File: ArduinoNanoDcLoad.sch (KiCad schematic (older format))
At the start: 30 parts, among them P1 CONN_01X15, P2 CONN_01X15, Q1 IRFP250N, U1 LMC6484

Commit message: * updated schematic
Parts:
- added C4: 10µ, Capacitors_ThroughHole:C_Radial_D10_L20_P5, symbol CP
- added C5, C7: 100n, Capacitors_ThroughHole:C_Rect_L4_W2.5_P2.5, symbol C
- added D2: 5,1V, Diodes_ThroughHole:Diode_DO-35_SOD27_Horizontal_RM10, symbol ZENER
- added P1: DCLOAD+, Connect:Banana_Jack_1Pin, symbol CONN_01X01
- added P2: DCLOAD-, Connect:Banana_Jack_1Pin, symbol CONN_01X01
- added R14: 10, Resistors_ThroughHole:Resistor_Horizontal_RM15mm, symbol R
- C1: footprint (none) -> Capacitors_ThroughHole:C_Radial_D10_L20_P5
- C2: value 100µ -> 100n; footprint (none) -> Capacitors_ThroughHole:C_Rect_L4_W2.5_P2.5
- C3: footprint (none) -> Capacitors_ThroughHole:C_Rect_L4_W2.5_P2.5
- C6: renamed from C4; footprint (none) -> Capacitors_ThroughHole:C_Rect_L4_W2.5_P2.5
- D1: footprint (none) -> Diodes_ThroughHole:Diode_DO-35_SOD27_Horizontal_RM10
- P3: renamed from P1; footprint (none) -> Pin_Headers:Pin_Header_Straight_1x15
- P4: renamed from P2; footprint (none) -> Pin_Headers:Pin_Header_Straight_1x15
- Q1: footprint (none) -> TO_SOT_Packages_THT:TO-247_Horizontal_Neutral123_largePads
- R1, R10, R11, R12, R13, R2, R3, R4, R8, R9: footprint (none) -> Resistors_ThroughHole:Resistor_Horizontal_RM15mm
- R15: renamed from R14; footprint (none) -> Resistors_ThroughHole:Resistor_Horizontal_RM15mm
- R16: renamed from R15; footprint (none) -> Resistors_ThroughHole:Resistor_Horizontal_RM15mm
- R17: renamed from R16; footprint (none) -> Resistors_ThroughHole:Resistor_Horizontal_RM15mm
- R18: renamed from R17; footprint (none) -> Resistors_ThroughHole:Resistor_Horizontal_RM15mm
- R19: renamed from R18; footprint (none) -> Resistors_ThroughHole:Resistor_Horizontal_RM15mm
- R20: renamed from R19; footprint (none) -> Resistors_ThroughHole:Resistor_Horizontal_RM15mm
- R21: renamed from R20; footprint (none) -> Resistors_ThroughHole:Resistor_Horizontal_RM15mm
- R22: renamed from R21; footprint (none) -> Resistors_ThroughHole:Resistor_Horizontal_RM15mm
- R5: renamed from R6; footprint (none) -> Resistors_ThroughHole:Resistor_Horizontal_RM15mm
- R6: renamed from R7; footprint (none) -> Resistors_ThroughHole:Resistor_Horizontal_RM15mm
- R7: renamed from R5; footprint (none) -> Resistors_ThroughHole:Resistor_Horizontal_RM15mm
- U1: footprint (none) -> Housings_DIP:DIP-14_W7.62mm_LongPads
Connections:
- net ADC_SPANNUNG is gone; now on net ADC7: C6.1, D1.1 (K), R18.1, R19.2
- net ADC_STROM is gone; now on net ADC6: R22.1
- net PWM_PIN9 is gone; now on net OC1A/PB1: R1.2
- net 3V3: now also P4.14 (P14); no longer P4.2 (P2)
- net 5V: now also P4.4 (P4); no longer P4.12 (P12)
- net ADC0/PC0: now also P4.12 (P12); no longer P4.4 (P4)
- net ADC1/PC1: now also P4.11 (P11); no longer P4.5 (P5)
- net ADC2/PC2: now also P4.10 (P10); no longer P4.6 (P6)
- net ADC3/PC3: now also P4.9 (P9); no longer P4.7 (P7)
- net ADC5/PC5/SCL: now also P4.7 (P7); no longer P4.9 (P9)
- net ADC6: now also P4.6 (P6), R21.1, R22.2, U1.8, C7.1, D2.1 (K); no longer P4.10 (P10)
- net ADC7: now also P4.5 (P5); no longer P4.11 (P11)
- net AREF: now also P4.13 (P13); no longer P4.3 (P3)
- net GND: now also P4.2 (P2), C5.2, C7.2, D2.2 (A), P2.1 (P1), R14.2; no longer P4.14 (P14)
- net RESET/PC6: now also P4.3 (P3); no longer P4.13 (P13)
- net SCK/PB5: now also P4.15 (P15); no longer P4.1 (P1)
- net VIN: now also P4.1 (P1); no longer P4.15 (P15)
- net LOAD_DC+: no longer names the net of Q1.2 (D), R18.2
- net LOAD_DC+: now also C4.1, C5.1, P1.1 (P1)
- new net: C4.2, R14.1
- no-connect marks 28 -> 23
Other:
- moved on the sheet: C6, D1, P3, P4, R18, R19, R22

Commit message: * updated
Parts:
- renumbered R15 to R14, R16 to R15, R17 to R16, R14 to R17
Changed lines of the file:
@@
 $EndComp
 $Comp
-L R R15
+L R R14
 U 1 1 5837BE8D
 P 5150 4250
-F 0 "R15" V 5230 4250 50  0000 C CNN
+F 0 "R14" V 5230 4250 50  0000 C CNN
 F 1 "1" V 5150 4250 50  0000 C CNN
 F 2 "Resistors_ThroughHole:Resistor_Horizontal_RM15mm" V 5080 4250 50  0001 C CNN
@@
 $EndComp
 $Comp
-L R R16
+L R R15
 U 1 1 5837BED2
 P 5300 4250
-F 0 "R16" V 5380 4250 50  0000 C CNN
+F 0 "R15" V 5380 4250 50  0000 C CNN
 F 1 "1" V 5300 4250 50  0000 C CNN
 F 2 "Resistors_ThroughHole:Resistor_Horizontal_RM15mm" V 5230 4250 50  0001 C CNN
@@
 $EndComp
 $Comp
-L R R17
+L R R16
 U 1 1 5837BF94
 P 5450 4250
-F 0 "R17" V 5530 4250 50  0000 C CNN
+F 0 "R16" V 5530 4250 50  0000 C CNN
 F 1 "1" V 5450 4250 50  0000 C CNN
 F 2 "Resistors_ThroughHole:Resistor_Horizontal_RM15mm" V 5380 4250 50  0001 C CNN
@@
 $EndComp
 $Comp
-L R R14
+L R R17
 U 1 1 5838940C
 P 5050 2300
-F 0 "R14" V 5130 2300 50  0000 C CNN
+F 0 "R17" V 5130 2300 50  0000 C CNN
 F 1 "10" V 5050 2300 50  0000 C CNN
 F 2 "Resistors_ThroughHole:Resistor_Horizontal_RM15mm" V 4980 2300 50  0001 C CNN

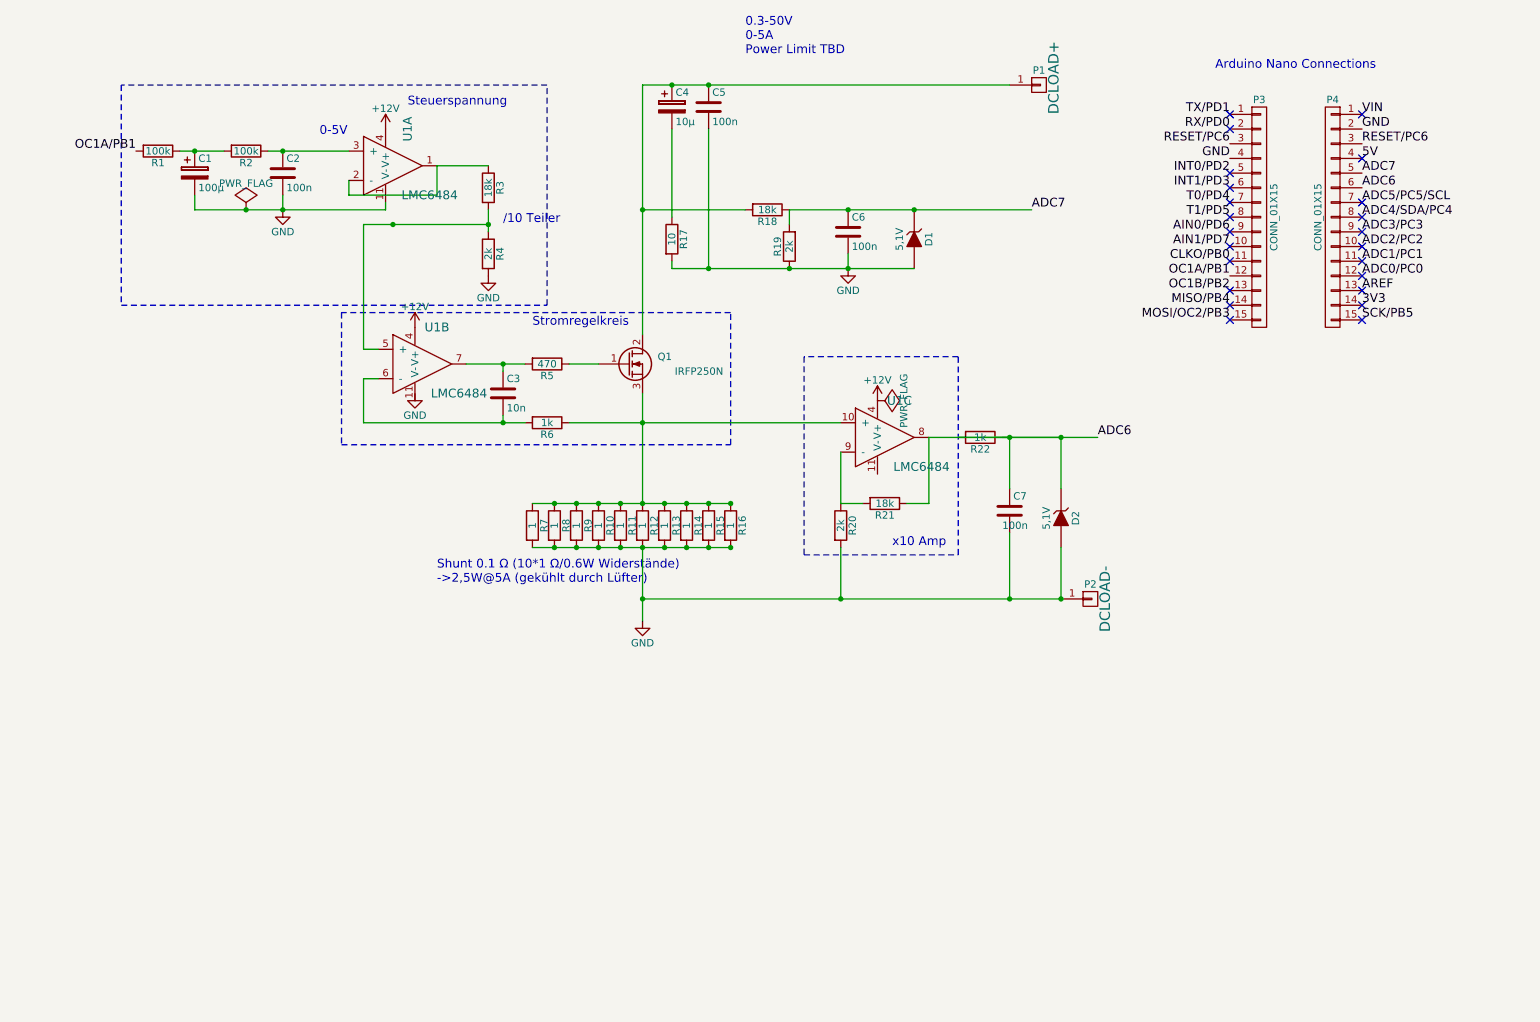
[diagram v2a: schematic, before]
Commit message: * added basic power supply * added LCD
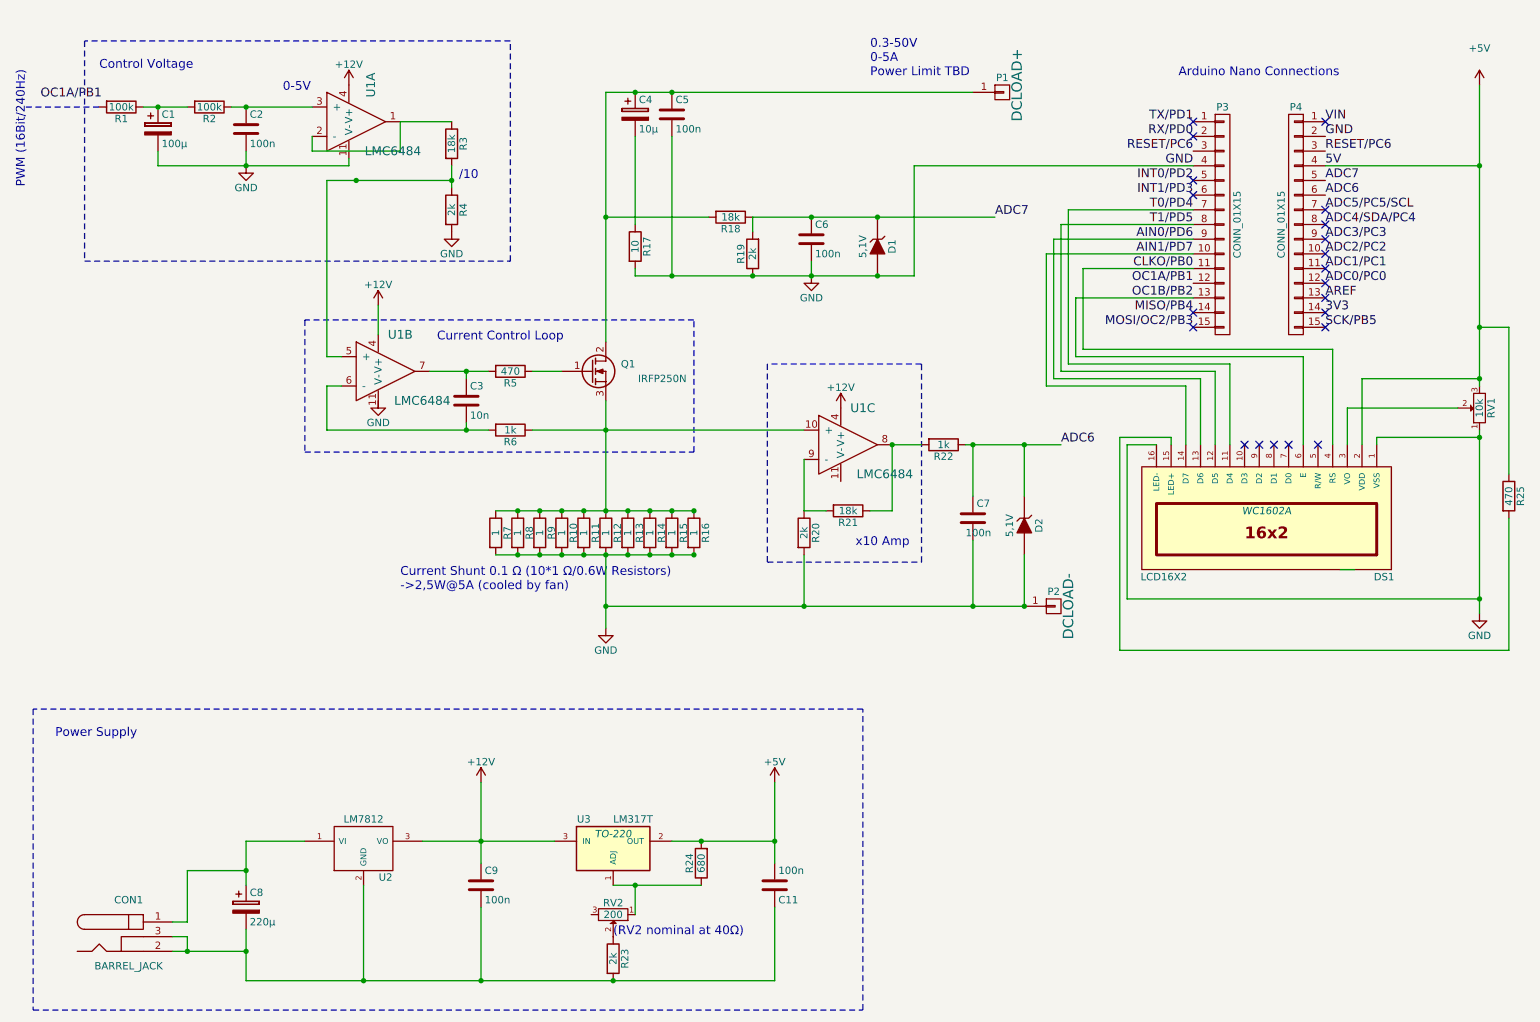
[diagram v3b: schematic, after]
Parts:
- added C11, C9: 100n, symbol C
- added C8: 220µ, symbol CP
- added CON1: BARREL_JACK, symbol BARREL_JACK
- added DS1: LCD16X2, WC1602A, symbol LCD16X2
- added R23: 2k, symbol R
- added R24: 680, symbol R
- added R25: 470, symbol R
- added RV1: 10k, symbol POT
- added RV2: 200, symbol POT
- added U2: LM7812, symbol LM7812
- added U3: LM317T, TO-220, symbol LM317T
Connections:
- net +12V: now also C9.1, U2.3 (VO), U3.3 (IN)
- net ADC6: no longer R21.1, R22.2, U1.8
- net AIN0/PD6: now also DS1.13 (D6)
- net AIN1/PD7: now also DS1.14 (D7)
- net CLKO/PB0: now also DS1.4 (RS)
- net GND: now also DS1.1 (VSS), DS1.16 (LED-), RV1.1
- net OC1A/PB1: no longer R1.2
- net OC1B/PB2: now also DS1.6 (E)
- net T0/PD4: now also DS1.11 (D4)
- net T1/PD5: now also DS1.12 (D5)
- net 5V renamed +5V
- net +5V: now also C11.2, DS1.2 (VDD), R24.2, R25.1, RV1.3, U3.2 (OUT)
- new net: R21.1, R22.2, U1.8
- new net: DS1.15 (LED+), R25.2
- new net: DS1.3 (VO), RV1.2
- new net: C8.1, CON1.1, U2.1 (VI)
- new net: C11.1, C8.2, C9.2, CON1.2, CON1.3, R23.2, U2.2 (GND)
- new net: R24.1, RV2.1, U3.1 (ADJ)
- new net: R23.1, RV2.2
- no-connect marks 23 -> 21
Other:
- note added: "(RV2 nominal at 40Ω)"
- note added: "/10"
- note added: "Control Voltage"
- note added: "Current Control Loop"
- note added: "Current Shunt 0.1 Ω (10*1 Ω/0.6W Resistors)\n->2,5W@5A (cooled by fan)\n"
- note added: "PWM (16Bit/240Hz)"
- note added: "Power Supply"
- note removed: "/10 Teiler"
- note removed: "Shunt 0.1 Ω (10*1 Ω/0.6W Widerstände)\n->2,5W@5A (gekühlt durch Lüfter)\n"
- note removed: "Steuerspannung"
- note removed: "Stromregelkreis"
- moved on the sheet: C1, C2, C3, C4, C5, C6, C7, D1, D2, P1, P2, P3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

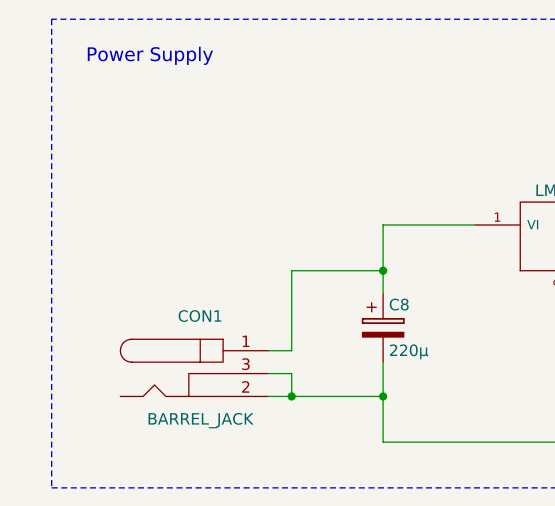
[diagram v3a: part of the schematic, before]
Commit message: added comment to schematic
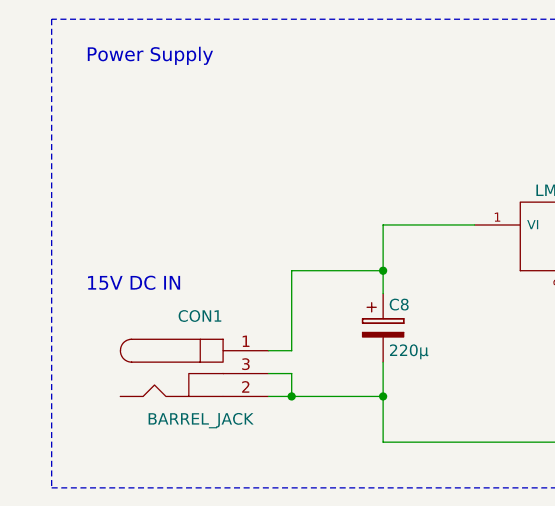
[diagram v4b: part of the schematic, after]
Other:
- note added: "15V DC IN"
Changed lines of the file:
@@
 	1750 6600 2150 6600
 Connection ~ 2150 6600
+Text Notes 850  6700 0    60   ~ 0
+15V DC IN
 $EndSCHEMATC

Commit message: * updated pcb layout
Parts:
- C11, C9: footprint (none) -> Capacitors_ThroughHole:C_Rect_L4_W2.5_P2.5
- C8: footprint (none) -> Capacitors_ThroughHole:C_Radial_D10_L20_P5
- CON1: footprint (none) -> Connect:JACK_ALIM
- DS1: footprint WC1602A -> Display:WC1602A
- R23, R24, R25: footprint (none) -> Resistors_ThroughHole:Resistor_Horizontal_RM15mm
- RV1, RV2: footprint (none) -> Potentiometers:Potentiometer_Trimmer-Piher-PT15-h5_vertical
- U2: footprint (none) -> TO_SOT_Packages_THT:TO-220_Neutral123_Vertical
- U3: footprint TO-220 -> TO_SOT_Packages_THT:TO-220_Neutral123_Vertical
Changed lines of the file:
@@
 	3550 1800 3550 1950
 $Comp
-L GND #PWR5
+L GND #PWR01
 U 1 1 5837A18E
 P 3550 2250
-F 0 "#PWR5" H 3550 2000 50  0001 C CNN
+F 0 "#PWR01" H 3550 2000 50  0001 C CNN
 F 1 "GND" H 3550 2100 50  0000 C CNN
 F 2 "" H 3550 2250 50  0000 C CNN
@@
 Connection ~ 3550 1900
 $Comp
-L GND #PWR9
+L GND #PWR02
 U 1 1 5837A566
 P 6000 2550
-F 0 "#PWR9" H 6000 2300 50  0001 C CNN
+F 0 "#PWR02" H 6000 2300 50  0001 C CNN
 F 1 "GND" H 6000 2400 50  0000 C CNN
 F 2 "" H 6000 2550 50  0000 C CNN
@@
 	4600 4450 4600 4950
 $Comp
-L GND #PWR7
+L GND #PWR03
 U 1 1 5837E175
 P 4600 4950
-F 0 "#PWR7" H 4600 4700 50  0001 C CNN
+F 0 "#PWR03" H 4600 4700 50  0001 C CNN
 F 1 "GND" H 4600 4800 50  0000 C CNN
 F 2 "" H 4600 4950 50  0000 C CNN
@@
 	3200 1700 3200 1500
 $Comp
-L GND #PWR1
+L GND #PWR04
 U 1 1 5838A7B7
 P 2150 1800
-F 0 "#PWR1" H 2150 1550 50  0001 C CNN
+F 0 "#PWR04" H 2150 1550 50  0001 C CNN
 F 1 "GND" H 2150 1650 50  0000 C CNN
 F 2 "" H 2150 1800 50  0000 C CNN
@@
 $EndComp
 $Comp
-L +12V #PWR2
+L +12V #PWR05
 U 1 1 5838A825
 P 2850 1250
-F 0 "#PWR2" H 2850 1100 50  0001 C CNN
+F 0 "#PWR05" H 2850 1100 50  0001 C CNN
 F 1 "+12V" H 2850 1390 50  0000 C CNN
 F 2 "" H 2850 1250 50  0000 C CNN
@@
 $EndComp
 $Comp
-L +12V #PWR10
+L +12V #PWR06
 U 1 1 5838A875
 P 6200 3450
-F 0 "#PWR10" H 6200 3300 50  0001 C CNN
+F 0 "#PWR06" H 6200 3300 50  0001 C CNN
 F 1 "+12V" H 6200 3590 50  0000 C CNN
 F 2 "" H 6200 3450 50  0000 C CNN
@@
 $EndComp
 $Comp
-L GND #PWR4
+L GND #PWR07
 U 1 1 5838AB96
 P 3050 3400
-F 0 "#PWR4" H 3050 3150 50  0001 C CNN
+F 0 "#PWR07" H 3050 3150 50  0001 C CNN
 F 1 "GND" H 3050 3250 50  0000 C CNN
 F 2 "" H 3050 3400 50  0000 C CNN
@@
 $EndComp
 $Comp
-L +12V #PWR3
+L +12V #PWR08
 U 1 1 5838AC69
 P 3050 2750
-F 0 "#PWR3" H 3050 2600 50  0001 C CNN
+F 0 "#PWR08" H 3050 2600 50  0001 C CNN
 F 1 "+12V" H 3050 2890 50  0000 C CNN
 F 2 "" H 3050 2750 50  0000 C CNN
@@
 F 0 "DS1" H 8300 4600 50  0000 C CNN
 F 1 "LCD16X2" H 9800 4600 50  0000 C CNN
-F 2 "WC1602A" H 9100 4150 50  0000 C CIN
+F 2 "Display:WC1602A" H 9100 4150 50  0000 C CIN
 F 3 "" H 9100 4200 50  0000 C CNN
 	1    9100 4200
@@
 $EndComp
 $Comp
-L +5V #PWR11
+L +5V #PWR09
 U 1 1 583D9119
 P 10550 1250
-F 0 "#PWR11" H 10550 1100 50  0001 C CNN
+F 0 "#PWR09" H 10550 1100 50  0001 C CNN
 F 1 "+5V" H 10550 1500 50  0000 C CNN
 F 2 "" H 10550 1250 50  0000 C CNN
@@
 F 0 "RV1" H 10550 3370 50  0000 C CNN
 F 1 "10k" H 10550 3450 50  0000 C CNN
-F 2 "" H 10550 3450 50  0000 C CNN
+F 2 "Potentiometers:Potentiometer_Trimmer-Piher-PT15-h5_vertical" H 10550 3450 50  0001 C CNN
 F 3 "" H 10550 3450 50  0000 C CNN
 	1    10550 3450
@@
 	9600 4550 9700 4550
 $Comp
-L GND #PWR12
+L GND #PWR010
 U 1 1 583DB5FD
 P 10550 4850
-F 0 "#PWR12" H 10550 4600 50  0001 C CNN
+F 0 "#PWR010" H 10550 4600 50  0001 C CNN
 F 1 "GND" H 10550 4700 50  0000 C CNN
 F 2 "" H 10550 4850 50  0000 C CNN
@@
 F 0 "CON1" H 1350 7300 50  0000 C CNN
 F 1 "BARREL_JACK" H 1350 6850 50  0000 C CNN
-F 2 "" H 1350 7050 50  0000 C CNN
+F 2 "Connect:JACK_ALIM" H 1350 7050 50  0001 C CNN
 F 3 "" H 1350 7050 50  0000 C CNN
 	1    1350 7050
@@
 F 0 "U2" H 3100 6254 50  0000 C CNN
 F 1 "LM7812" H 2950 6650 50  0000 C CNN
-F 2 "" H 2950 6450 50  0000 C CNN
+F 2 "TO_SOT_Packages_THT:TO-220_Neutral123_Vertical" H 2950 6450 50  0001 C CNN
 F 3 "" H 2950 6450 50  0000 C CNN
 	1    2950 6450
@@
 F 0 "C9" H 3775 6800 50  0000 L CNN
 F 1 "100n" H 3775 6600 50  0000 L CNN
-F 2 "" H 3788 6550 50  0000 C CNN
+F 2 "Capacitors_ThroughHole:C_Rect_L4_W2.5_P2.5" H 3788 6550 50  0001 C CNN
 F 3 "" H 3750 6700 50  0000 C CNN
 	1    3750 6700
@@
 F 0 "C11" H 5775 6800 50  0000 L CNN
 F 1 "100n" H 5775 6600 50  0000 L CNN
-F 2 "" H 5788 6550 50  0000 C CNN
+F 2 "Capacitors_ThroughHole:C_Rect_L4_W2.5_P2.5" H 5788 6550 50  0001 C CNN
 F 3 "" H 5750 6700 50  0000 C CNN
 	1    5750 6700
@@
 F 0 "U3" H 4450 6650 50  0000 C CNN
 F 1 "LM317T" H 4650 6650 50  0000 L CNN
-F 2 "TO-220" H 4650 6550 50  0000 C CIN
+F 2 "TO_SOT_Packages_THT:TO-220_Neutral123_Vertical" H 4650 6550 50  0001 C CIN
 F 3 "" H 4650 6450 50  0000 C CNN
 	1    4650 6450
@@
 F 0 "R24" V 5330 6550 50  0000 C CNN
 F 1 "680" V 5250 6550 50  0000 C CNN
-F 2 "" V 5180 6550 50  0000 C CNN
+F 2 "Resistors_ThroughHole:Resistor_Horizontal_RM15mm" V 5180 6550 50  0001 C CNN
 F 3 "" H 5250 6550 50  0000 C CNN
 	1    5250 6550
@@
 F 0 "RV2" H 4650 6820 50  0000 C CNN
 F 1 "200" H 4650 6900 50  0000 C CNN
-F 2 "" H 4650 6900 50  0000 C CNN
+F 2 "Potentiometers:Potentiometer_Trimmer-Piher-PT15-h5_vertical" H 4650 6900 50  0001 C CNN
 F 3 "" H 4650 6900 50  0000 C CNN
 	1    4650 6900
@@
 F 0 "R23" V 4730 7200 50  0000 C CNN
 F 1 "2k" V 4650 7200 50  0000 C CNN
-F 2 "" V 4580 7200 50  0000 C CNN
+F 2 "Resistors_ThroughHole:Resistor_Horizontal_RM15mm" V 4580 7200 50  0001 C CNN
 F 3 "" H 4650 7200 50  0000 C CNN
 	1    4650 7200
@@
 Connection ~ 3750 6400
 $Comp
-L +12V #PWR6
+L +12V #PWR011
 U 1 1 5840112A
 P 3750 6000
-F 0 "#PWR6" H 3750 5850 50  0001 C CNN
+F 0 "#PWR011" H 3750 5850 50  0001 C CNN
 F 1 "+12V" H 3750 6140 50  0000 C CNN
 F 2 "" H 3750 6000 50  0000 C CNN
@@
 Connection ~ 5750 6400
 $Comp
-L +5V #PWR8
+L +5V #PWR012
 U 1 1 584076AC
 P 5750 6000
-F 0 "#PWR8" H 5750 5850 50  0001 C CNN
+F 0 "#PWR012" H 5750 5850 50  0001 C CNN
 F 1 "+5V" H 5750 6140 50  0000 C CNN
 F 2 "" H 5750 6000 50  0000 C CNN
@@
 F 0 "R25" V 10830 4050 50  0000 C CNN
 F 1 "470" V 10750 4050 50  0000 C CNN
-F 2 "" V 10680 4050 50  0000 C CNN
+F 2 "Resistors_ThroughHole:Resistor_Horizontal_RM15mm" V 10680 4050 50  0001 C CNN
 F 3 "" H 10750 4050 50  0000 C CNN
 	1    10750 4050
@@
 F 0 "C8" H 2175 6950 50  0000 L CNN
 F 1 "220µ" H 2175 6750 50  0000 L CNN
-F 2 "" H 2188 6700 50  0000 C CNN
+F 2 "Capacitors_ThroughHole:C_Radial_D10_L20_P5" H 2188 6700 50  0001 C CNN
 F 3 "" H 2150 6850 50  0000 C CNN
 	1    2150 6850

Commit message: * update
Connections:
- net at R21.1, R22.2: now also U1.14; no longer U1.8
- net at R20.1, R21.2: now also U1.13 (-); no longer U1.9 (-)
- net at Q1.3 (S), R10.1, R11.1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: now also U1.12 (+); no longer U1.10 (+)
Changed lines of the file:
@@
 $Comp
 L LMC6484 U1
-U 3 1 583779F2
+U 4 1 583779F2
 P 6150 3700
 F 0 "U1" H 6350 3950 60  0000 C CNN
@@
 F 2 "Housings_DIP:DIP-14_W7.62mm_LongPads" H 6100 3850 60  0001 C CNN
 F 3 "" H 6100 3850 60  0001 C CNN
-	3    6150 3700
+	4    6150 3700
 	1    0    0    -1
 $EndComp
